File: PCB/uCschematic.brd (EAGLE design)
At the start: 80 x 75 mm, 62 parts, among them IC1 PIC24FJXXGA002/SO, IC10 ULN2003D1013TR, IC11 ULN2003D1013TR, IC12 ULN2003D1013TR, IC13 FT230XS-U, IC2 317EMP, IC3 MC74HC175ADG, IC4 MC74HC175ADG, IC5 MC74HC175ADG, IC6 MC74HC175ADG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

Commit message: Dodan kondenzator većeg kapaciteta na ulazu za napajanje
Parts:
- added C20: 100u, eagle-ltspice:C0805
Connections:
- net 12V: now also C20.2
- net GND: now also C20.1
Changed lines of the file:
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@@
 <drawing>
 <settings>
-<setting alwaysvectorfont="yes"/>
+<setting alwaysvectorfont="no"/>
 <setting verticaltext="up"/>
 </settings>
@@
 <attribute name="VALUE" x="8.3" y="43.3408" size="1.27" layer="27" rot="R270"/>
 </element>
+<element name="C20" library="eagle-ltspice" library_urn="urn:adsk.eagle:library:217" package="C0805" package3d_urn="urn:adsk.eagle:package:13265/1" value="100u" x="9.5" y="36.5" smashed="yes" rot="MR180">
+<attribute name="NAME" x="8.23" y="35.23" size="1.27" layer="26" rot="MR180"/>
+<attribute name="SPICEMODEL" value="NONE" x="9.5" y="36.5" size="1.778" layer="28" rot="MR180" display="off"/>
+<attribute name="SPICEPREFIX" value="C" x="9.5" y="36.5" size="1.778" layer="28" rot="MR180" display="off"/>
+<attribute name="VALUE" x="8.23" y="39.04" size="1.27" layer="28" rot="MR180"/>
+</element>
 </elements>
 <signals>
@@
 <contactref element="C2" pad="1"/>
 <contactref element="IC1" pad="27"/>
+<contactref element="C20" pad="1"/>
 </signal>
 <signal name="N$3">
@@
 <contactref element="MOTOR5" pad="5"/>
 <contactref element="MOTOR6" pad="5"/>
+<contactref element="C20" pad="2"/>
 <wire x1="67.89" y1="3.82" x2="71.755" y2="13.378" width="0" layer="19" extent="16-16"/>
 <wire x1="54.84" y1="3.82" x2="67.89" y2="3.82" width="0" layer="19" extent="1-1"/>
@@
 <wire x1="2.34" y1="3.63" x2="15.39" y2="3.63" width="0" layer="19" extent="1-1"/>
 <wire x1="12.3712" y1="33.6114" x2="19.165728125" y2="12.962178125" width="0" layer="19" extent="16-16"/>
-<wire x1="13.02" y1="41.8" x2="12.3712" y2="33.6114" width="0" layer="19" extent="16-16"/>
-<wire x1="4.88" y1="41.98" x2="13.02" y2="41.8" width="0" layer="19" extent="16-16"/>
+<wire x1="10.45" y1="36.5" x2="12.3712" y2="33.6114" width="0" layer="19" extent="16-16"/>
+<wire x1="13.02" y1="41.8" x2="10.45" y2="36.5" width="0" layer="19" extent="16-16"/>
+<wire x1="4.88" y1="41.98" x2="10.45" y2="36.5" width="0" layer="19" extent="16-16"/>
 </signal>
 <signal name="GP_OKIDAC">

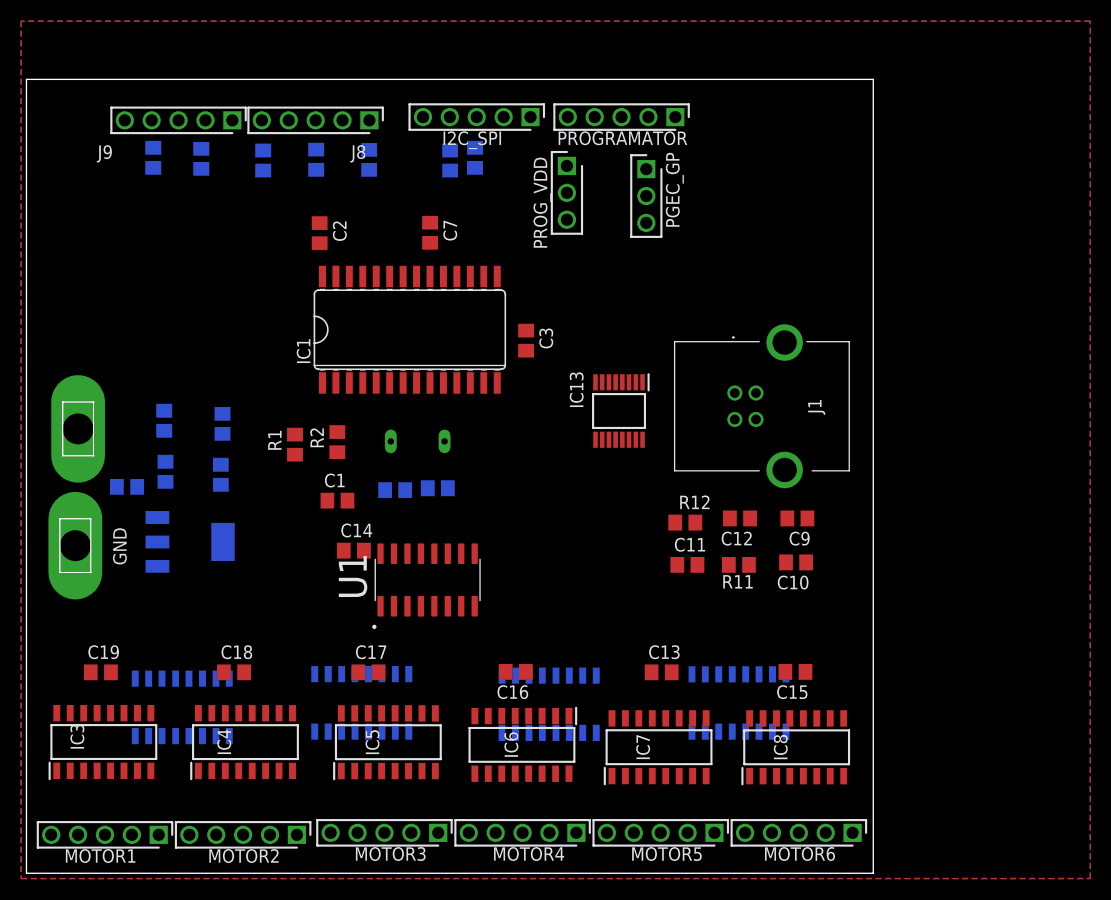
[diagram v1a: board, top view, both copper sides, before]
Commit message: - Rutiranje kontrolera za upravljanje stepper motorima  - Dodavanje DRC fajla za dvoslojni PCB
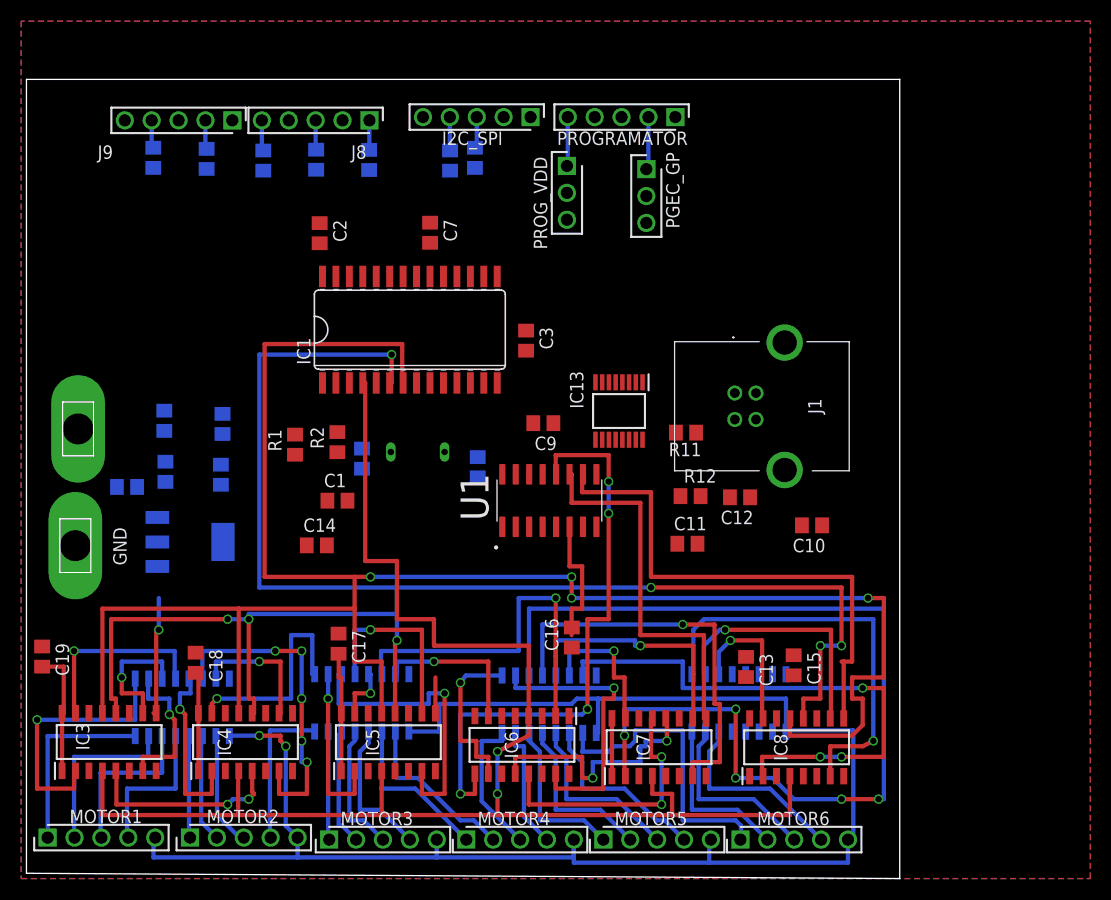
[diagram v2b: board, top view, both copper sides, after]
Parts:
- moved C9 25.6 mm to (48.8, 42.5)
- moved U1 13.7 mm to (49.4, 35.2)
- moved R11 13.5 mm to (62.3, 41.6)
- moved MOTOR6 10.6 mm to (67.5, 3.18), turned to 0 degrees
- moved MOTOR5 10.5 mm to (54.5, 3.18), turned to 0 degrees
- moved MOTOR1 10.5 mm to (2.00, 3.37), turned to 0 degrees
- moved MOTOR4 10.4 mm to (41.5, 3.18), turned to 0 degrees
- moved MOTOR3 10.3 mm to (28.6, 3.18), turned to 0 degrees
- moved MOTOR2 10.1 mm to (15.4, 3.37), turned to 0 degrees
- moved C13 7.99 mm to (68.0, 19.5), turned to 270 degrees
- moved C16 6.21 mm to (51.5, 22.3), turned to 90 degrees
- moved C19 5.75 mm to (1.48, 20.5), turned to 270 degrees
- moved C6 4.31 mm to (31.7, 39.2), turned to 90 degrees
- moved C8 4.26 mm to (42.6, 38.4), turned to 90 degrees
- moved C17 3.92 mm to (29.5, 21.7), turned to 270 degrees
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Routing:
- net N$12: track 0.00 -> 207.9 mm, vias 0 -> 6
- net N$13: track 0.00 -> 190.7 mm, vias 0 -> 9
- net 12V: track 0.00 -> 157.2 mm, vias 0 -> 2
- net N$19: track 0.00 -> 147.2 mm, vias 0 -> 2
- net M4_0: track 0.00 -> 96.1 mm, vias 0 -> 5
- net M3: track 0.00 -> 55.8 mm, vias 0 -> 4
- net M5_0: track 0.00 -> 52.2 mm, vias 0 -> 3
- net 3.3V: track 0.00 -> 51.2 mm
- net M5: track 0.00 -> 49.6 mm
- net M5_1: track 0.00 -> 40.3 mm, vias 0 -> 1
- net M4_1: track 0.00 -> 38.5 mm, vias 0 -> 1
- net M4: track 0.00 -> 36.0 mm
- net M3_0: track 0.00 -> 34.9 mm, vias 0 -> 1
- net M1_1: track 0.00 -> 30.8 mm, vias 0 -> 5
- net N$68: track 0.00 -> 28.2 mm
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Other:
- board size 80 x 75 mm -> 82.5 x 75.5 mm

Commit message: Rutiranje USB -a, graničnih prekidača i regulatora napona.
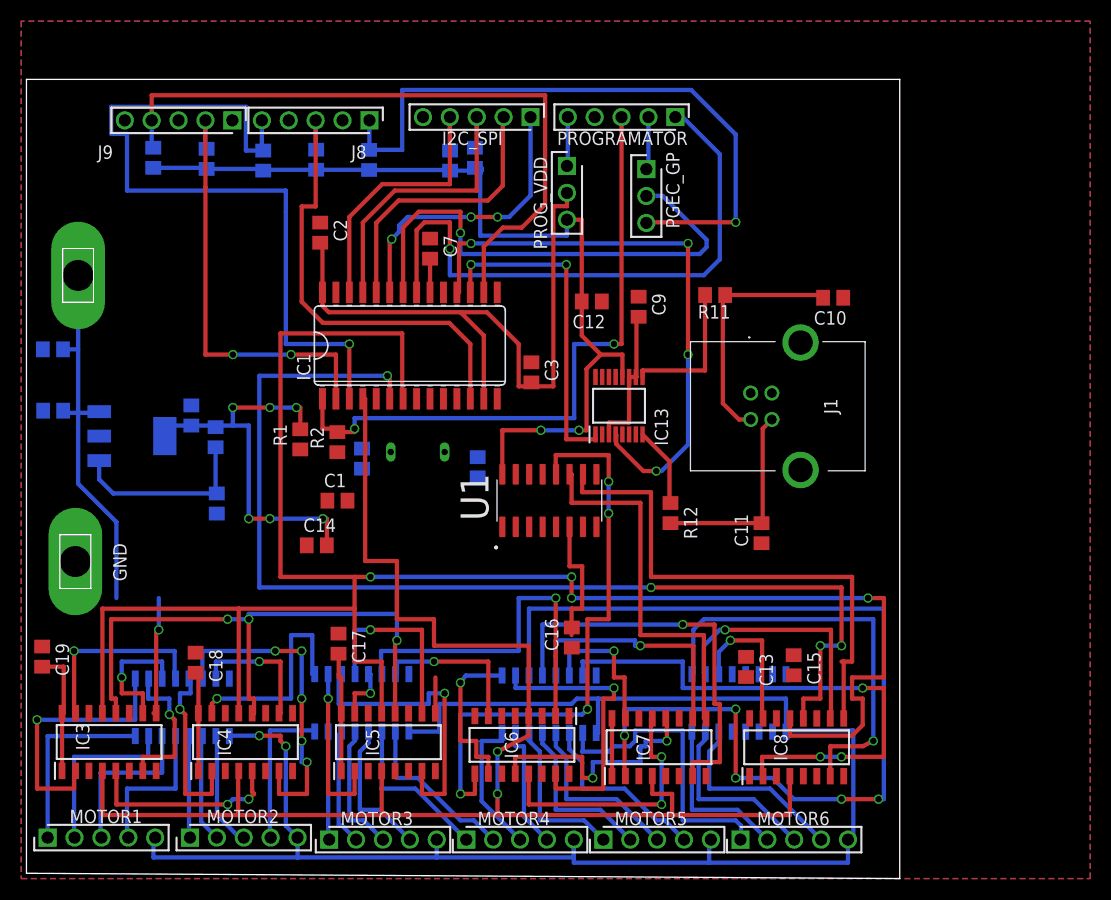
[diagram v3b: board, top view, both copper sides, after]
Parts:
- moved C12 23.2 mm to (53.4, 54.0)
- moved C10 21.6 mm to (76.2, 54.4)
- moved C20 14.8 mm to (2.50, 49.5)
- moved VDD 14.5 mm to (4.88, 56.5)
- moved C9 14.2 mm to (57.8, 53.5), turned to 270 degrees
- moved R11 13.3 mm to (65.1, 54.6)
- moved IC2 11.4 mm to (9.97, 41.3)
- moved C5 10.5 mm to (2.52, 43.7), turned to 180 degrees
- moved C11 7.07 mm to (69.4, 32.1), turned to 90 degrees
- moved R4 5.70 mm to (18.0, 34.9), turned to 90 degrees
- moved R3 3.59 mm to (17.9, 41.2), turned to 90 degrees
- moved C4 3.06 mm to (15.6, 43.2)
- moved C3 3.04 mm to (47.7, 47.3)
- moved R12 2.48 mm to (60.8, 34.0), turned to 270 degrees
- moved C7 1.50 mm to (38.1, 59.0)
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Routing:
- net 3.3V: track 51.2 -> 177.7 mm, vias 0 -> 8
- net N$29: track 2.90 -> 71.5 mm, vias 0 -> 1
- net N$4: track 0.00 -> 62.5 mm
- net N$38: track 2.65 -> 64.3 mm
- net N$2: track 0.00 -> 61.2 mm, vias 0 -> 2
- net GP_OKIDAC: track 2.80 -> 61.6 mm, vias 0 -> 1
- net N$7: track 0.00 -> 56.0 mm, vias 0 -> 1
- net N$25: track 0.00 -> 55.3 mm, vias 0 -> 4
- net N$24: track 0.00 -> 47.8 mm, vias 0 -> 1
- net N$17: track 2.79 -> 44.0 mm
- net N$37: track 3.62 -> 42.2 mm, vias 0 -> 2
- net 12V: track 157.2 -> 194.2 mm
- net N$26: track 0.00 -> 31.4 mm, vias 0 -> 2
- net N$39: track 0.00 -> 27.7 mm, vias 0 -> 3
- net N$40: track 0.00 -> 26.5 mm
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
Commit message: Valjda gotovo
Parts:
- moved GND 28.5 mm to (7.08, 57.9)
- moved C14 26.3 mm to (53.7, 30.7), turned to 90 degrees
- moved R11 21.9 mm to (75.0, 35.2), turned to 90 degrees
- moved R3 18.9 mm to (18.1, 60.1), turned to 0 degrees
- moved R12 18.2 mm to (79.0, 35.3), turned to 90 degrees
- moved C12 18.0 mm to (68.2, 43.8), turned to 270 degrees
- moved C4 16.9 mm to (13.9, 60.1), turned to 180 degrees
- moved IC11 16.1 mm to (56.2, 30.6)
- moved C9 15.9 mm to (70.5, 43.8)
- moved J1 15.4 mm to (88.7, 56.3)
- moved IC12 15.2 mm to (71.9, 30.6)
- moved IC9 14.9 mm to (14.6, 30.6)
- moved C10 14.8 mm to (75.0, 39.6), turned to 270 degrees
- moved IC13 14.5 mm to (68.8, 37.4)
- moved IC10 14.5 mm to (31.2, 30.6)
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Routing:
- net 3.3V: track 177.7 -> 284.2 mm, vias 8 -> 3
- net N$18: track 18.8 -> 113.0 mm, vias 2 -> 6
- net N$12: track 208.4 -> 130.9 mm, vias 6 -> 3
- net N$13: track 187.8 -> 116.8 mm, vias 9 -> 7
- net N$67: track 17.4 -> 76.8 mm, vias 0 -> 3
- net M4_0: track 96.1 -> 40.3 mm, vias 5 -> 3
- net M0: track 11.2 -> 62.8 mm, vias 1 -> 4
- net N$16: track 0.00 -> 46.3 mm, vias 0 -> 2
- net 12V: track 194.2 -> 239.3 mm, vias 2 -> 0
- net N$29: track 71.5 -> 32.6 mm, vias 1 -> 0
- net N$49: track 12.5 -> 48.6 mm, vias 0 -> 4
- net N$64: track 15.4 -> 47.9 mm, vias 0 -> 2
- net N$65: track 16.0 -> 46.9 mm, vias 0 -> 4
- net N$63: track 11.8 -> 41.5 mm, vias 0 -> 2
- net M3: track 55.8 -> 26.7 mm
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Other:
- board size 82.5 x 75.5 mm -> 90 x 80 mm
